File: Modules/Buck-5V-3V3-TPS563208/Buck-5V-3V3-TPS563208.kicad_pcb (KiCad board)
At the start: 4 copper layers, 13 parts, among them U8 TPS563208

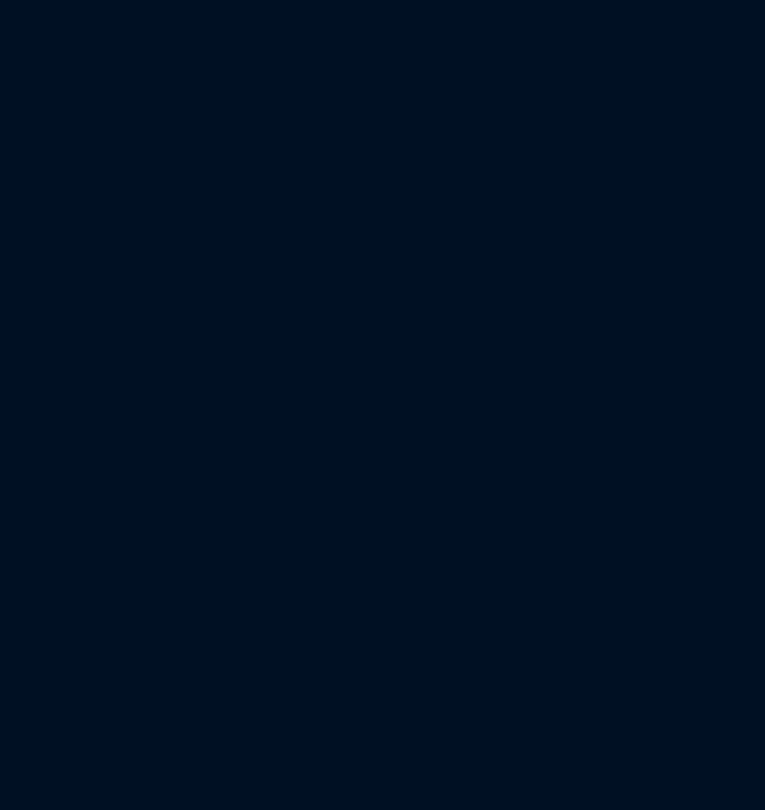
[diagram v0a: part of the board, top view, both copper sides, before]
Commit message: Add the base zones to five module boards
Whole-board zones for USBC, Buck, PowerMux, MCU and RF, written by file
before each board is opened. RF In1 carries a notch under J3 pad 1. Power
polygons become wide tracks during layout, because add_copper_pour cannot
set a zone priority.

Co-Authored-By: Claude Opus 5.5 (1M context) <noreply@anthropic.com>
Claude-Session: https://claude.ai/code/session_01ErAAfkmF4h3T5yfrw21utF
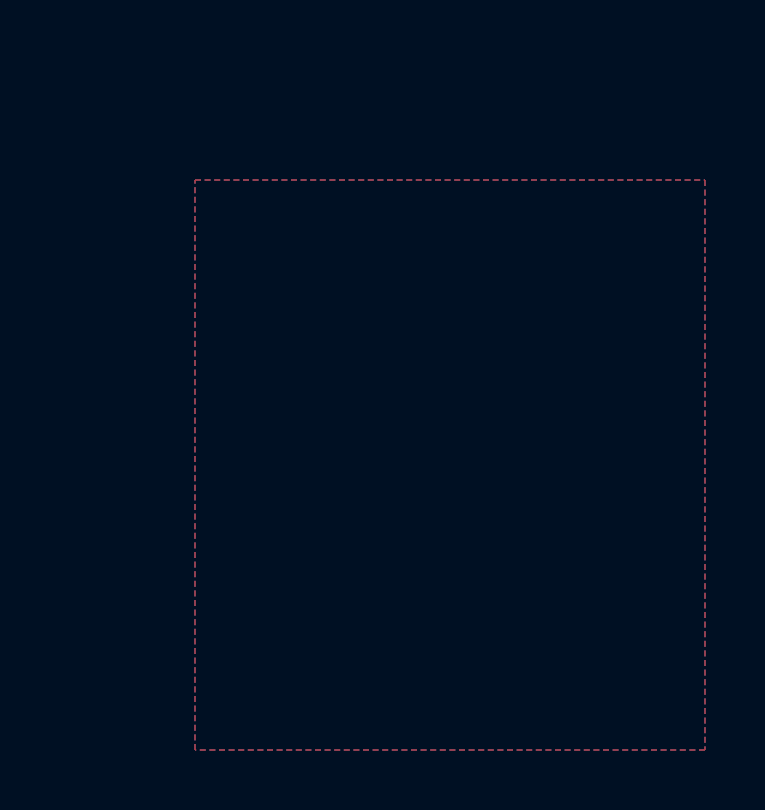
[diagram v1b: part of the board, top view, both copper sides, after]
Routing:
- added copper zone on In2.Cu, net /V5_SYS
- added copper zone on B.Cu, net GND
- added copper zone on F.Cu, net GND
- added copper zone on In1.Cu, net GND
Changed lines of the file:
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@@
 	)
 	(embedded_fonts no)
-)
+  (zone (net 0) (net_name "GND") (layer "F.Cu")
+    (hatch edge 0.508)
+    (connect_pads (clearance 0.2))
+    (min_thickness 0.25)
+    (fill yes)
+    (polygon (pts
+      (xy 100.5 100.5)
+      (xy 117.5 100.5)
+      (xy 117.5 119.5)
+      (xy 100.5 119.5)
+    ))
+  )
+  (zone (net 0) (net_name "GND") (layer "In1.Cu")
+    (hatch edge 0.508)
+    (connect_pads (clearance 0.2))
+    (min_thickness 0.25)
+    (fill yes)
+    (polygon (pts
+      (xy 100.5 100.5)
+      (xy 117.5 100.5)
+      (xy 117.5 119.5)
+      (xy 100.5 119.5)
+    ))
+  )
+  (zone (net 0) (net_name "/V5_SYS") (layer "In2.Cu")
+    (hatch edge 0.508)
+    (connect_pads (clearance 0.2))
+    (min_thickness 0.25)
+    (fill yes)
+    (polygon (pts
+      (xy 100.5 100.5)
+      (xy 117.5 100.5)
+      (xy 117.5 119.5)
+      (xy 100.5 119.5)
+    ))
+  )
+  (zone (net 0) (net_name "GND") (layer "B.Cu")
+    (hatch edge 0.508)
+    (connect_pads (clearance 0.2))
+    (min_thickness 0.25)
+    (fill yes)
+    (polygon (pts
+      (xy 100.5 100.5)
+      (xy 117.5 100.5)
+      (xy 117.5 119.5)
+      (xy 100.5 119.5)
+    ))
+  ))

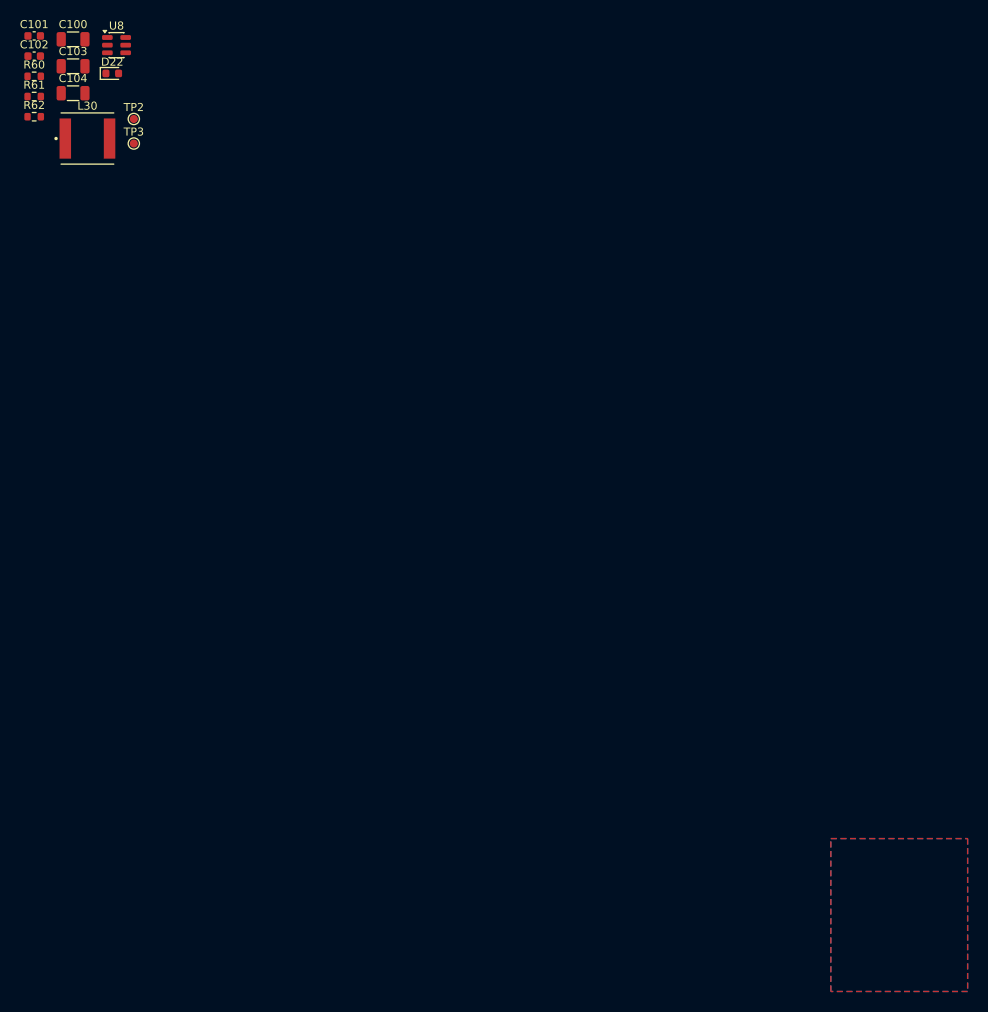
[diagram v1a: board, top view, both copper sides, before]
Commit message: Lay out the Buck-5V-3V3-TPS563208 module
18 x 20 mm, 4 layers. C101 sits under U8.3 and C100 (now 22 uF 1206) beside
it, so the input loop stays short. The SW node is a 0.6 x 2.2 mm strip and
C102 joins it over L30. C103 and C104 share one +3V3 trunk to the row.
Breakout row at y 117.5: three +3V3, three V5_SYS and four GND vias.

DRC: 0 errors, 0 unconnected, 0 parity. The 6 track_dangling warnings are
the 6 interface stubs. Canary 35 to 182.

Co-Authored-By: Claude Opus 5.5 (1M context) <noreply@anthropic.com>
Claude-Session: https://claude.ai/code/session_01ErAAfkmF4h3T5yfrw21utF
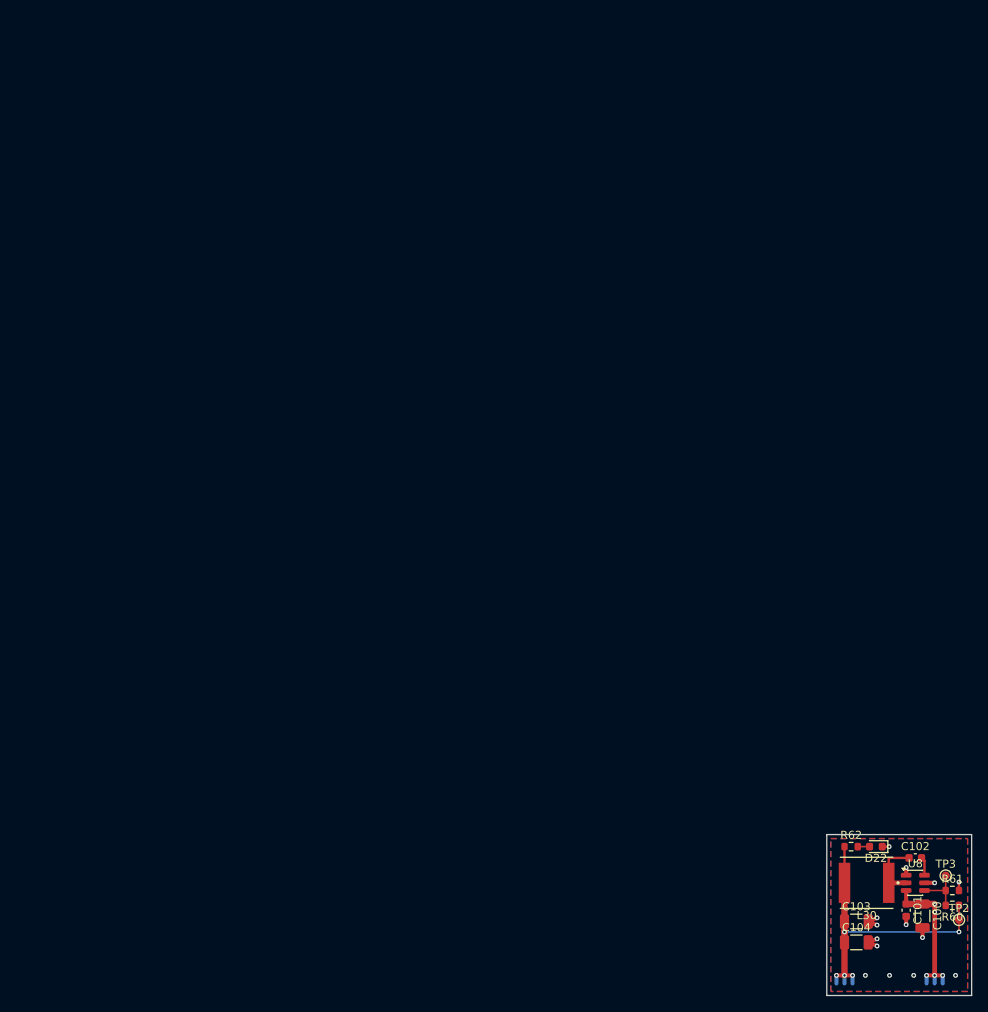
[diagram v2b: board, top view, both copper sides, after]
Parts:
- moved R60 153.7 mm to (115.6, 108.8), turned to 180 degrees
- moved C101 153.4 mm to (109.9, 109.4), turned to -90 degrees
- moved C100 151.7 mm to (111.9, 110.1), turned to -90 degrees
- moved R61 150.8 mm to (115.6, 107.0)
- moved C102 148.0 mm to (111.0, 102.9)
- moved C103 144.1 mm to (103.7, 110.8)
- moved U8 143.8 mm to (111.0, 106.0)
- moved C104 143.6 mm to (103.7, 113.4)
- moved TP2 142.9 mm to (116.4, 110.6)
- moved R62 136.1 mm to (103.0, 101.5)
- moved TP3 135.9 mm to (114.8, 105.1)
- moved D22 135.0 mm to (106.1, 101.5), turned to 180 degrees
- moved L30 133.9 mm to (105.0, 106.0), turned to 180 degrees
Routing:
- net +3V3: track 0.00 -> 38.5 mm, vias 0 -> 5
- net /V5_SYS: track 0.00 -> 20.4 mm, vias 0 -> 6
- net GND: track 0.00 -> 9.87 mm, vias 0 -> 13
- net /SW_NODE: track 0.00 -> 7.79 mm
- net /VFB_33: track 0.00 -> 6.34 mm
- net /VBST: track 0.00 -> 2.30 mm
- net /LED_PWR_A: track 0.00 -> 1.46 mm
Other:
- board outline added: 18 x 20 mm
- board text added: "+3V3"
- board text added: "GND"
- board text added: "V5_SYS"

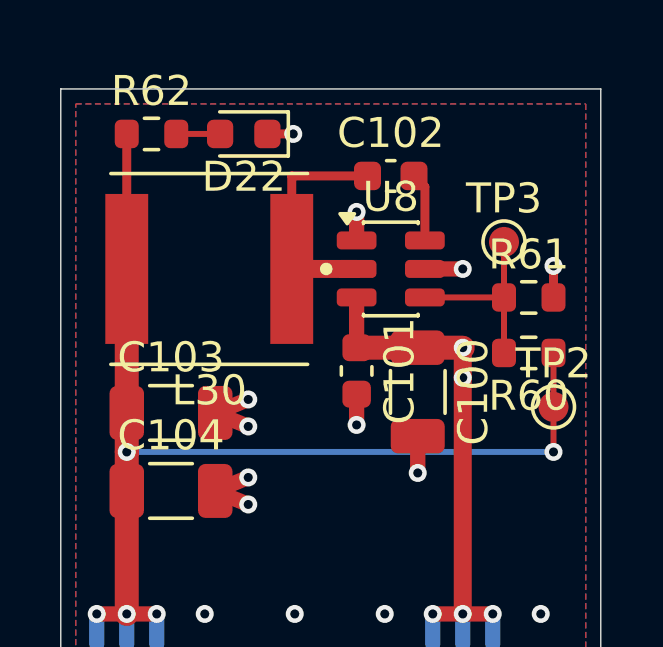
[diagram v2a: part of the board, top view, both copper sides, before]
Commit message: Restore footprints and move passive references to F.Fab
GUI batch 2a on all eight module boards. Update Footprints from Library
restores the (units) blocks that Konnect IPC writes dropped: U10, U1, SW1,
SW2 and U4 no longer report lib_footprint_mismatch. Reference designators of
C, R, L, FB, D, Y and TP parts move to F.Fab. U, J and SW stay on the silk.

Every board: DRC 0 errors, 0 unconnected, 0 parity, the canary fires, and
track_dangling equals the interface stub count.

Co-Authored-By: Claude Opus 5.5 (1M context) <noreply@anthropic.com>
Claude-Session: https://claude.ai/code/session_01ErAAfkmF4h3T5yfrw21utF
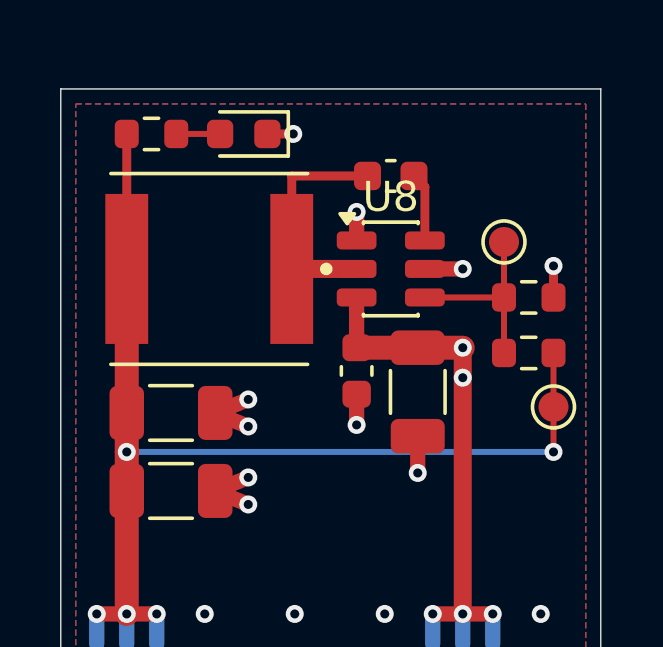
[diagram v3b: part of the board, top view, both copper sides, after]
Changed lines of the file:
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@@
 		(property "Reference" "TP3"
 			(at 0 -1.448 0)
-			(layer "F.SilkS")
+			(layer "F.Fab")
 			(effects
 				(font
@@
 		(property "Reference" "R61"
 			(at 0 -1.43 0)
-			(layer "F.SilkS")
+			(layer "F.Fab")
 			(effects
 				(font
@@
 		(property "Reference" "R62"
 			(at 0 -1.43 0)
-			(layer "F.SilkS")
+			(layer "F.Fab")
 			(effects
 				(font
@@
 		(property "Reference" "C102"
 			(at 0 -1.43 0)
-			(layer "F.SilkS")
+			(layer "F.Fab")
 			(effects
 				(font
@@
 		(tags "capacitor")
 		(property "Reference" "C100"
-			(at 0 -1.85 -90)
-			(layer "F.SilkS")
+			(at 0 -1.85 270)
+			(layer "F.Fab")
 			(effects
 				(font
@@
 		)
 		(property "Value" "22uF 16V X5R"
-			(at 0 1.85 -90)
+			(at 0 1.85 270)
 			(layer "F.Fab")
 			(effects
@@
 		)
 		(property "Datasheet" ""
-			(at 0 0 -90)
+			(at 0 0 270)
 			(layer "F.Fab")
 			(hide yes)
@@
 		)
 		(property "Description" ""
-			(at 0 0 -90)
+			(at 0 0 270)
 			(layer "F.Fab")
 			(hide yes)
@@
 		)
 		(property "KiLib_Generator" "SMD_2terminal_chip_molded"
-			(at 0 0 -90)
+			(at 0 0 270)
 			(layer "F.SilkS")
 			(hide yes)
@@
 		)
 		(property "MPN" "FCC1206X226K160HT"
-			(at 0 0 -90)
+			(at 0 0 270)
 			(unlocked yes)
 			(layer "F.Fab")
@@
 		)
 		(property "Manufacturer" "Fenghua"
-			(at 0 0 -90)
+			(at 0 0 270)
 			(unlocked yes)
 			(layer "F.Fab")
@@
 		)
 		(fp_text user "${REFERENCE}"
-			(at 0 0 -90)
+			(at 0 0 270)
 			(layer "F.Fab")
 			(effects
@@
 		(property "Reference" "C104"
 			(at 0 -1.85 0)
-			(layer "F.SilkS")
+			(layer "F.Fab")
 			(effects
 				(font
@@
 		(tags "capacitor")
 		(property "Reference" "C101"
-			(at 0 -1.43 -90)
-			(layer "F.SilkS")
+			(at 0 -1.43 270)
+			(layer "F.Fab")
 			(effects
 				(font
@@
 		)
 		(property "Value" "100nF"
-			(at 0 1.43 -90)
+			(at 0 1.43 270)
 			(layer "F.Fab")
 			(effects
@@
 		)
 		(property "Datasheet" ""
-			(at 0 0 -90)
+			(at 0 0 270)
 			(layer "F.Fab")
 			(hide yes)
@@
 		)
 		(property "Description" ""
-			(at 0 0 -90)
+			(at 0 0 270)
 			(layer "F.Fab")
 			(hide yes)
@@
 		)
 		(property "KiLib_Generator" "SMD_2terminal_chip_molded"
-			(at 0 0 -90)
+			(at 0 0 270)
 			(layer "F.SilkS")
 			(hide yes)
@@
 		)
 		(property "MPN" "GRM188R71H104KA93D"
-			(at 0 0 -90)
+			(at 0 0 270)
 			(unlocked yes)
 			(layer "F.Fab")
@@
 		)
 		(property "Manufacturer" "Murata"
-			(at 0 0 -90)
+			(at 0 0 270)
 			(unlocked yes)
 			(layer "F.Fab")
@@
 		)
 		(fp_text user "${REFERENCE}"
-			(at 0 0 -90)
+			(at 0 0 270)
 			(layer "F.Fab")
 			(effects
@@
 		(property "Reference" "D22"
 			(at 0 -1.43 180)
-			(layer "F.SilkS")
+			(layer "F.Fab")
 			(effects
 				(font
@@
 		(property "Reference" "R60"
 			(at 0 -1.43 180)
-			(layer "F.SilkS")
+			(layer "F.Fab")
 			(effects
 				(font
@@
 		(property "Reference" "TP2"
 			(at 0 -1.448 0)
-			(layer "F.SilkS")
+			(layer "F.Fab")
 			(effects
 				(font
@@
 		(property "Reference" "C103"
 			(at 0 -1.85 0)
-			(layer "F.SilkS")
+			(layer "F.Fab")
 			(effects
 				(font
@@
 		(property "Reference" "L30"
 			(at 0 -4.05 180)
-			(layer "F.SilkS")
-			(effects
-				(font
+			(layer "F.Fab")
+			(effects
+				(font

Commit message: Apply the review fixes to five boards and set solid power pads
Plans were proven on scratch copies, then applied with KiCad's own pcbnew
Python API, so KiCad writes every file. Each board: DRC 0 errors, 0
unconnected, 0 parity, and the canary fires.

Ethernet and PoE module (R1-1, R1-2, R1-3):
- The fanout rule no longer matches zones.
- Chip-side copper keeps 1.0 mm from the line-side jack pads (was 0.26 mm):
  MDI_RDP, MDI_RDN, RCT and LED_LINK_K rerouted. A 1.0 mm rule enforces it.
  The VC1P lane passes J2.8 at 0.42 mm inside the jack pad field, and only
  that pair is excepted.
- GND vias: Ethernet 8 to 42, PoE 11 to 55. No starved thermal remains.

Buck (R2-2, R2-5): three GND vias at U8.1, C100.2 and C101.2. TP3 sits
against R61.1, with a courtyard rule scoped to that pair.
USBC (R2-4): U2 moves 3 mm toward J1, with two GND vias at U2.2.
MCU (R1-9): C2 sits 1.71 mm from U1 pin 3 (was 23.5 mm), with a courtyard
rule scoped to C2 and U1.
Solid zone connections (R2-3) on U8, L30, C100 to C104, C108 to C111 and J1.

Co-Authored-By: Claude Opus 5.5 (1M context) <noreply@anthropic.com>
Claude-Session: https://claude.ai/code/session_01ErAAfkmF4h3T5yfrw21utF
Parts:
- moved TP3 0.85 mm to (114.8, 106.0)
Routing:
- net GND: track 9.87 -> 14.9 mm, vias 13 -> 19
- net /VFB_33: track 6.34 -> 5.49 mm
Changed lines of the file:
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@@
 	(footprint "TestPoint:TestPoint_Pad_D1.0mm"
 		(layer "F.Cu")
-		(at 114.775 105.1)
+		(at 114.775 105.95)
 		(descr "SMD pad as test Point, diameter 1.0mm")
 		(tags "test point SMD pad")
@@
 		(sheetname "/")
 		(sheetfile "Buck-5V-3V3-TPS563208.kicad_sch")
+		(zone_connect 2)
 		(attr smd)
 		(duplicate_pad_numbers_are_jumpers no)
@@
 		(sheetname "/")
 		(sheetfile "Buck-5V-3V3-TPS563208.kicad_sch")
+		(zone_connect 2)
 		(attr smd)
 		(duplicate_pad_numbers_are_jumpers no)
@@
 		(sheetname "/")
 		(sheetfile "Buck-5V-3V3-TPS563208.kicad_sch")
+		(zone_connect 2)
 		(attr smd)
 		(duplicate_pad_numbers_are_jumpers no)
@@
 		(sheetname "/")
 		(sheetfile "Buck-5V-3V3-TPS563208.kicad_sch")
+		(zone_connect 2)
 		(attr smd)
 		(duplicate_pad_numbers_are_jumpers no)
@@
 		(sheetname "/")
 		(sheetfile "Buck-5V-3V3-TPS563208.kicad_sch")
+		(zone_connect 2)
 		(attr smd)
 		(duplicate_pad_numbers_are_jumpers no)
@@
 		(sheetname "/")
 		(sheetfile "Buck-5V-3V3-TPS563208.kicad_sch")
+		(zone_connect 2)
 		(attr smd)
 		(duplicate_pad_numbers_are_jumpers no)
@@
 		(sheetname "/")
 		(sheetfile "Buck-5V-3V3-TPS563208.kicad_sch")
+		(zone_connect 2)
 		(attr smd)
 		(duplicate_pad_numbers_are_jumpers no)
@@
 	(segment
 		(start 114.775 106.95)
-		(end 114.775 105.1)
+		(end 114.775 105.95)
 		(width 0.2)
 		(layer "F.Cu")
@@
 	)
 	(segment
+		(start 109.8625 104.1)
+		(end 109 104.1)
+		(width 0.508)
+		(layer "F.Cu")
+		(net "GND")
+	)
+	(segment
 		(start 105.15 110.8)
 		(end 106.25 110.35)
@@
 	)
 	(segment
+		(start 109.8625 104.1)
+		(end 110.75 104.1)
+		(width 0.508)
+		(layer "F.Cu")
+		(net "GND")
+	)
+	(segment
 		(start 105.15 113.4)
 		(end 106.25 112.95)
@@
 	)
 	(segment
+		(start 111.9 112.8)
+		(end 111.2 112.8)
+		(width 0.508)
+		(layer "F.Cu")
+		(net "GND")
+	)
+	(segment
+		(start 109.8625 110.175)
+		(end 108.95 110.175)
+		(width 0.508)
+		(layer "F.Cu")
+		(net "GND")
+	)
+	(segment
 		(start 105.15 110.8)
 		(end 106.25 111.25)
@@
 		(start 111.9 111.575)
 		(end 111.9 112.8)
+		(width 0.508)
+		(layer "F.Cu")
+		(net "GND")
+	)
+	(segment
+		(start 111.9 112.8)
+		(end 112.6 112.8)
+		(width 0.508)
+		(layer "F.Cu")
+		(net "GND")
+	)
+	(segment
+		(start 108.95 110.175)
+		(end 108.85 109.25)
 		(width 0.508)
 		(layer "F.Cu")
@@
 	)
 	(via
+		(at 109 104.1)
+		(size 0.6)
+		(drill 0.3)
+		(layers "F.Cu" "B.Cu")
+		(net "GND")
+	)
+	(via
 		(at 116 117.5)
+		(size 0.6)
+		(drill 0.3)
+		(layers "F.Cu" "B.Cu")
+		(net "GND")
+	)
+	(via
+		(at 112.6 112.8)
 		(size 0.6)
 		(drill 0.3)
@@
 	)
 	(via
+		(at 108.95 110.175)
+		(size 0.6)
+		(drill 0.3)
+		(layers "F.Cu" "B.Cu")
+		(net "GND")
+	)
+	(via
+		(at 110.75 104.1)
+		(size 0.6)
+		(drill 0.3)
+		(layers "F.Cu" "B.Cu")
+		(net "GND")
+	)
+	(via
 		(at 106.25 113.85)
 		(size 0.6)
@@
 	)
 	(via
+		(at 108.85 109.25)
+		(size 0.6)
+		(drill 0.3)
+		(layers "F.Cu" "B.Cu")
+		(net "GND")
+	)
+	(via
 		(at 116.425 105.9)
 		(size 0.6)
 		(drill 0.3)
+		(layers "F.Cu" "B.Cu")
+		(net "GND")
+	)
+	(via
+		(at 111.2 112.8)
+		(size 0.6)
+		(drill 0.3)
